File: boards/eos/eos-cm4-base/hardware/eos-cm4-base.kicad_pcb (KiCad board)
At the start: 4 copper layers, 90 x 80 mm, 43 parts, among them J1 CM4 1-100, J2 CM4 101-200, J3 USB-C, J4 USB-A, J5 TRJG0926HENL, J6 microSD, J7 GPIO, J8 FAN, J9 BOOT, Q1 BSS84, SW1 RESET, U1 USBLC6-2SC6, U2 TPS2041B, U3 USBLC6-2SC6, U4 TPD4EUSB30, U5 TPD4EUSB30, U6 RT9742GGJ5, U7 TS3USB30E

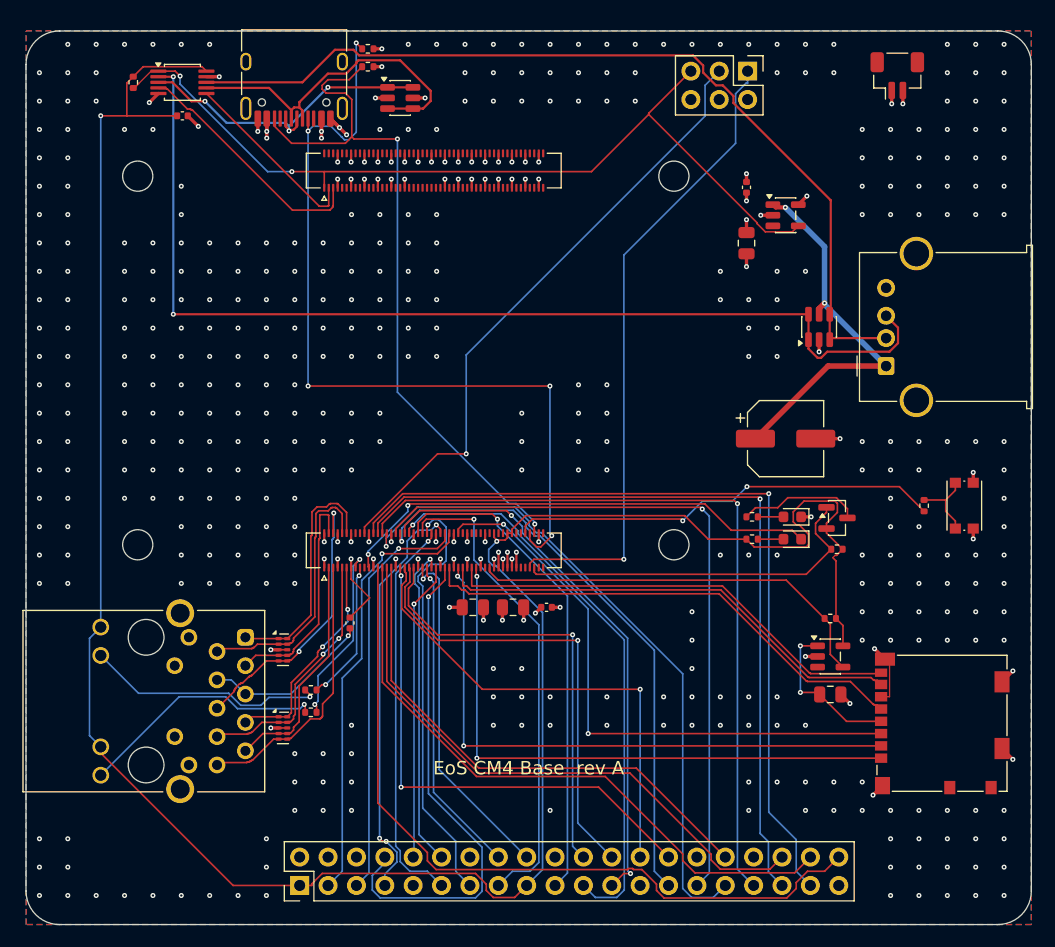
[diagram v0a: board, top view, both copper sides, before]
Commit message: feat(boards): EoS Motion Wing and EoS ESP32 DevKit; CM4 USB rework; build fixes
Two more original boards, for catalogue entries whose CAD can't be mirrored. Both were drafted
from chip datasheets and published form-factor specs (no vendor design file), then built and
independently reviewed:
- EoS Motion Wing, a FeatherWing. ADXL343 and ADT7410 on I2C, removable pull-ups,
  address/interrupt jumpers. The outline and headers come from Adafruit's Feather spec. New
  symbol EoS_Sensors:ADT7410 (pins from the ADT7410 datasheet Rev. C, Table 4).
- EoS ESP32 DevKit. ESP32-WROOM-32E with KiCad's own symbol, its stacked GND pin expanded to
  four pads. CP2102N with the esptool auto-program pair, AP7361C. A PMEG6010CEH and a 5.1 kohm
  bleed keep VBUS below the CP2102N's VIL with no host.

EoS CM4 Base, after review:
- The USB-A port moved to the top edge, beside the module's USB pins. The host path fell from
  116/98 mm to 46/35 mm (TI's limit is 101.6 mm).
- USB-A power now comes from a TPS2051C driven through a 2N7002, so it is on only in host mode
  and only with the CM4's 3.3 V up. The old active-low switch turned on when that rail was down.
- 0.1 uF at the switch output, as in TI's application circuit.
- The README now covers the OS's otg_mode and dr_mode, 5 V / 3 A, and the HAT back-feed warning.

Generator fixes, each found on these boards:
- Stacked pin numbers: strict parsing and expansion.
- KiCad's no-connect net names ({slash}, unnamed pins).
- Pre-routes and repairs at the net class width.
- ROUTER_MARGIN 0.01 mm, and necks below the minimum widened (locked copper excepted).
- Clearance clashes between routed items ripped up and repaired.
- Silkscreen stroke at least 0.15 mm.

Tests:
- SpecTest, ClashTest, and FigureFourTest: the carriers' holes and connectors placed from
  Figure 4's dimensions alone.
- Intent tests for the CM4, Motion Wing and ESP32.
- Every board README's results table checked against its build report.

All built boards: ERC 0, DRC errors 0, 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
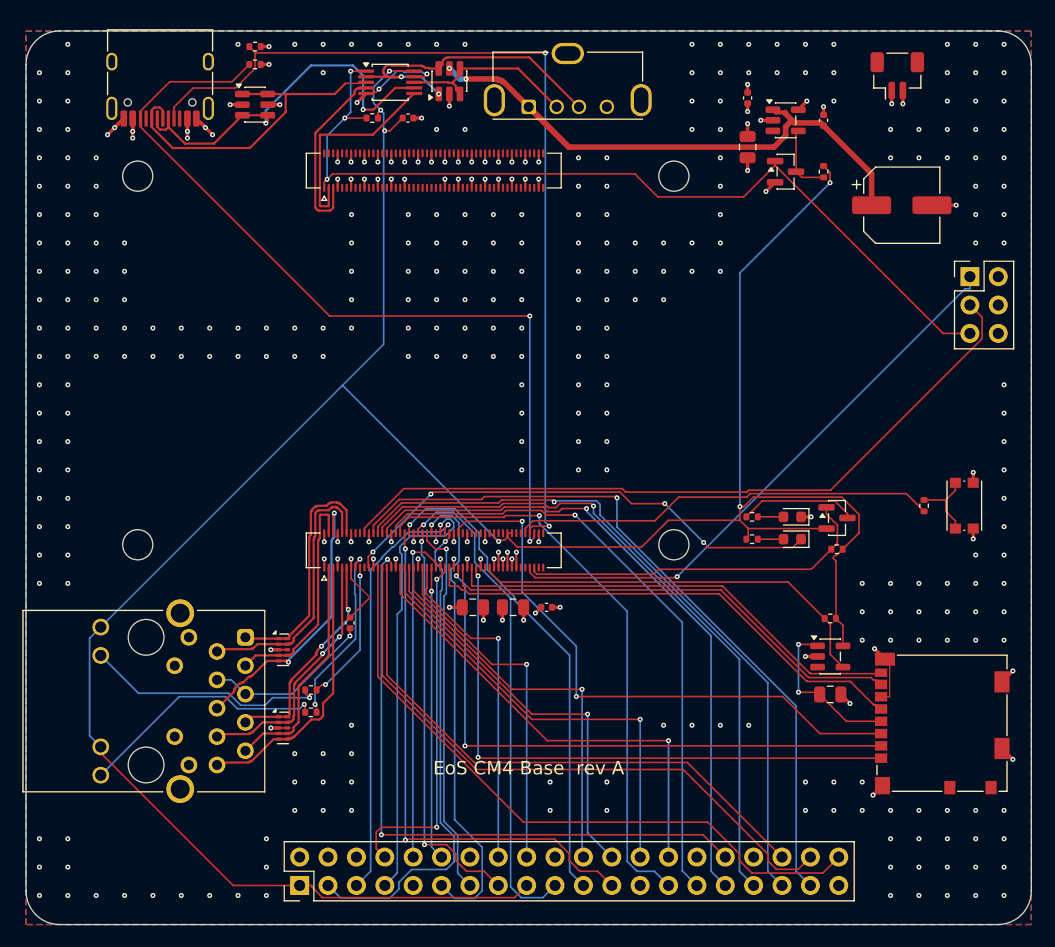
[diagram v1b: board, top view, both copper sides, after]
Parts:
- added C10: 100n, Capacitor_SMD:C_0402_1005Metric, F.Cu at (71.4, 8.00)
- added Q2: 2N7002, Package_TO_SOT_SMD:SOT-23, F.Cu at (68.0, 12.6)
- added R11: 10k, Resistor_SMD:R_0402_1005Metric, F.Cu at (71.4, 12.6)
- J4: footprint Connector_USB:USB_A_Molex_67643_Horizontal -> Connector_USB:USB_A_Molex_105057_Vertical
- U2: value TPS2041B -> TPS2051C
- moved U3 39.7 mm to (37.9, 4.50)
- moved J4 39.5 mm to (45.0, 6.80), turned to 0 degrees
- moved J9 27.1 mm to (84.5, 22.0), turned to 0 degrees
- moved C6 23.3 mm to (78.4, 15.6)
- moved R10 21.6 mm to (31.0, 7.80), turned to 0 degrees
- moved C9 20.2 mm to (34.2, 7.80)
- moved U7 18.6 mm to (32.6, 4.60)
- moved U1 13.0 mm to (20.5, 6.60)
- moved J3 12.0 mm to (12.0, 3.80)
- moved R6 10.1 mm to (20.5, 1.40)
- moved R7 10.1 mm to (20.5, 3.00)
- moved C5 8.60 mm to (64.6, 10.4)
- moved U2 8.50 mm to (68.0, 8.00)
- moved C4 8.00 mm to (64.6, 6.00)
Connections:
- U2 pad 4: /OTG_ID -> /USBH_EN
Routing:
- net /USBH_DP: track 94.3 -> 29.6 mm
- net /USBH_DM: track 81.0 -> 16.4 mm
- net +3V3: track 208.6 -> 236.4 mm, vias 2 -> 6
- net /USBH_VBUS: track 34.7 -> 54.2 mm
- net /GPIO14: track 45.4 -> 31.7 mm, vias 1 -> 2
- net /CC2: track 64.4 -> 75.9 mm
- net /GPIO12: track 46.6 -> 57.4 mm, vias 0 -> 2
- net /EEPROM_NWP: track 56.0 -> 66.5 mm, vias 1 -> 0
- net /GPIO21: track 68.5 -> 59.3 mm
- net GND: track 84.2 -> 93.3 mm, vias 463 -> 364
- net /GPIO19: track 71.6 -> 62.6 mm
- net /GPIO26: track 74.0 -> 65.5 mm
- net /GPIO5: track 63.1 -> 55.1 mm
- net /GPIO9: track 51.8 -> 43.9 mm
- net /GPIO13: track 68.4 -> 60.6 mm
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
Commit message: fix(boards): USB-C at HRO's edge distance on EoS CM4 Base and EoS ESP32 DevKit
Both now place their HRO TYPE-C-31-M-12 at design.USB_C_EDGE (3.19 mm from
the edge it faces), as the first four boards do since d6baf98: at 3.8 mm the
shell's face sat 0.15 mm behind the board edge, so a plug's overmold could
meet the board before the plug seated.

Rebuilt: EoS CM4 Base ERC 0, DRC errors 0, unconnected 0, parity 0, 4 DRC
warnings; EoS ESP32 DevKit the same with 8 warnings, as before.
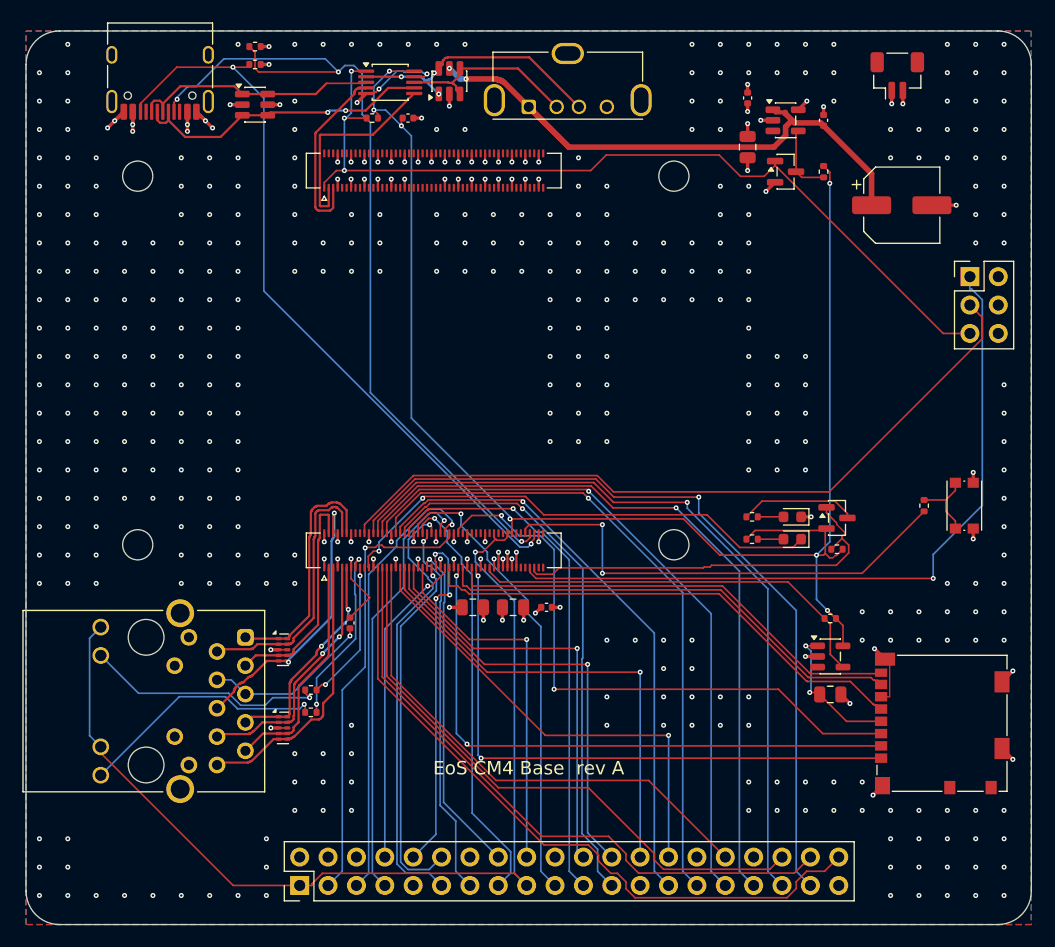
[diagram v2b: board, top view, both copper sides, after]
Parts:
- moved J3 0.61 mm to (12.0, 3.19)
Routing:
- net /NRPIBOOT: track 51.8 -> 66.1 mm
- net /GPIO12: track 57.4 -> 46.3 mm, vias 2 -> 0
- net /USBC_DP: track 30.7 -> 22.3 mm
- net /CC2: track 75.9 -> 67.7 mm
- net /USBC_DM: track 34.3 -> 27.1 mm
- net /GPIO19: track 62.6 -> 68.8 mm
- net +3V3: track 236.4 -> 230.2 mm, vias 6 -> 8
- net /GPIO18: track 26.3 -> 32.3 mm
- net /GPIO26: track 65.5 -> 71.4 mm
- net /GPIO13: track 60.6 -> 66.2 mm
- net /USBH_DP: track 29.6 -> 24.4 mm, vias 2 -> 3
- net /RUN_PG: track 38.1 -> 42.9 mm, vias 0 -> 2
- net /GPIO2: track 44.2 -> 40.1 mm
- net /PI_LED_NPWR: track 32.4 -> 35.9 mm
- net /GPIO14: track 31.7 -> 28.3 mm, vias 2 -> 1
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
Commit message: fix(boards): rebuild the ten boards made before the no-via-in-pad rule (#55)
PR #64's generator keeps vias out of surface pads (a chip's exposed pad
aside) and 0.1 mm from their own net's pads. Ten boards on master were built
before that rule and had 34 pads with a via in or beside them. They are
rebuilt with the same generator: ATmega328P, RA2E1, KE16Z, KL25, STM32 64,
ESP32 DevKit, Learn RP2350, LPC55S69, CM4 Base and CM5 Base. Each builds at
ERC 0, DRC errors 0, unconnected 0 and parity 0, with the same parts, values,
nets and positions and the same DRC warnings as before.

Where the router could no longer close a short link without a via in a pad,
or left a ground pad without a good path to a via, the design files use
routing options only: priority routes, fanout_first, ground_vias, and a
bottom-layer router keep-out under KL25's crystal (so RESET_b no longer runs
under it). ViaInPadTest drops BUILT_BEFORE_THE_RULE; it now allows only Learn
RP2350's two Raspberry Pi reference vias, named by position. READMEs, TASKS
and CHANGELOG follow the rebuilt copper. Independent verification: three
rounds; the owner adopted a two-layer pour-island criterion (TASKS.md).

Part of #55.
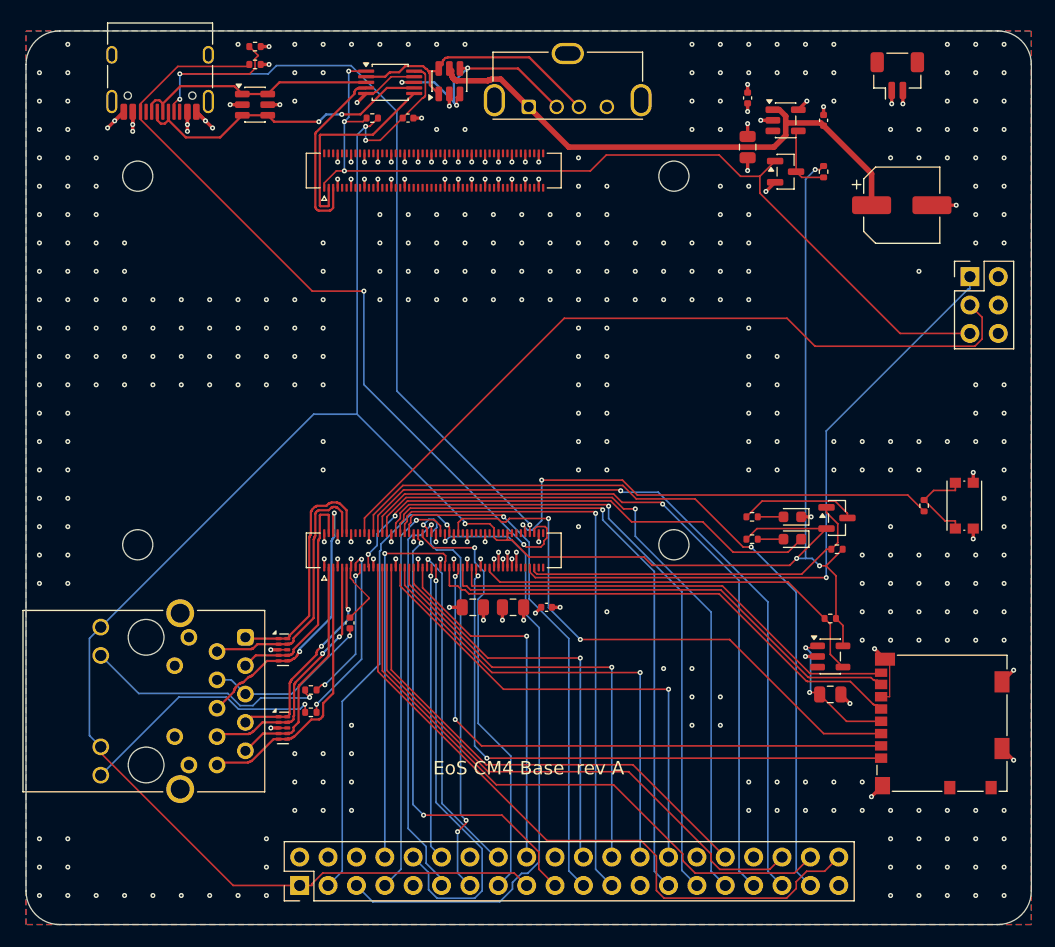
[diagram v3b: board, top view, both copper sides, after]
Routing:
- net /GPIO3: track 40.4 -> 55.6 mm
- net /GPIO15: track 31.3 -> 39.5 mm, vias 3 -> 1
- net /NRPIBOOT: track 66.1 -> 59.5 mm
- net /USBH_DM: track 16.4 -> 22.4 mm, vias 0 -> 3
- net /GPIO18: track 32.3 -> 26.3 mm
- net /GPIO14: track 28.3 -> 33.8 mm
- net /CC2: track 67.7 -> 72.7 mm
- net /USBH_VBUS: track 54.2 -> 49.4 mm, vias 2 -> 0
- net /GPIO27: track 33.6 -> 38.1 mm, vias 1 -> 3
- net /GPIO17: track 39.3 -> 35.6 mm
- net /ID_SD: track 52.4 -> 56.0 mm
- net /PI_LED_NPWR: track 35.9 -> 32.4 mm
- net /GPIO11: track 49.3 -> 52.6 mm
- net +3V3: track 230.2 -> 232.9 mm, vias 8 -> 6
- net /SD_CMD: track 54.3 -> 51.9 mm
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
